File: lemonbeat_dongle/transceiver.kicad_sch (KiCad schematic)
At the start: 21 parts, among them J301 SMA, U301 Si4467, Y301 26MHz

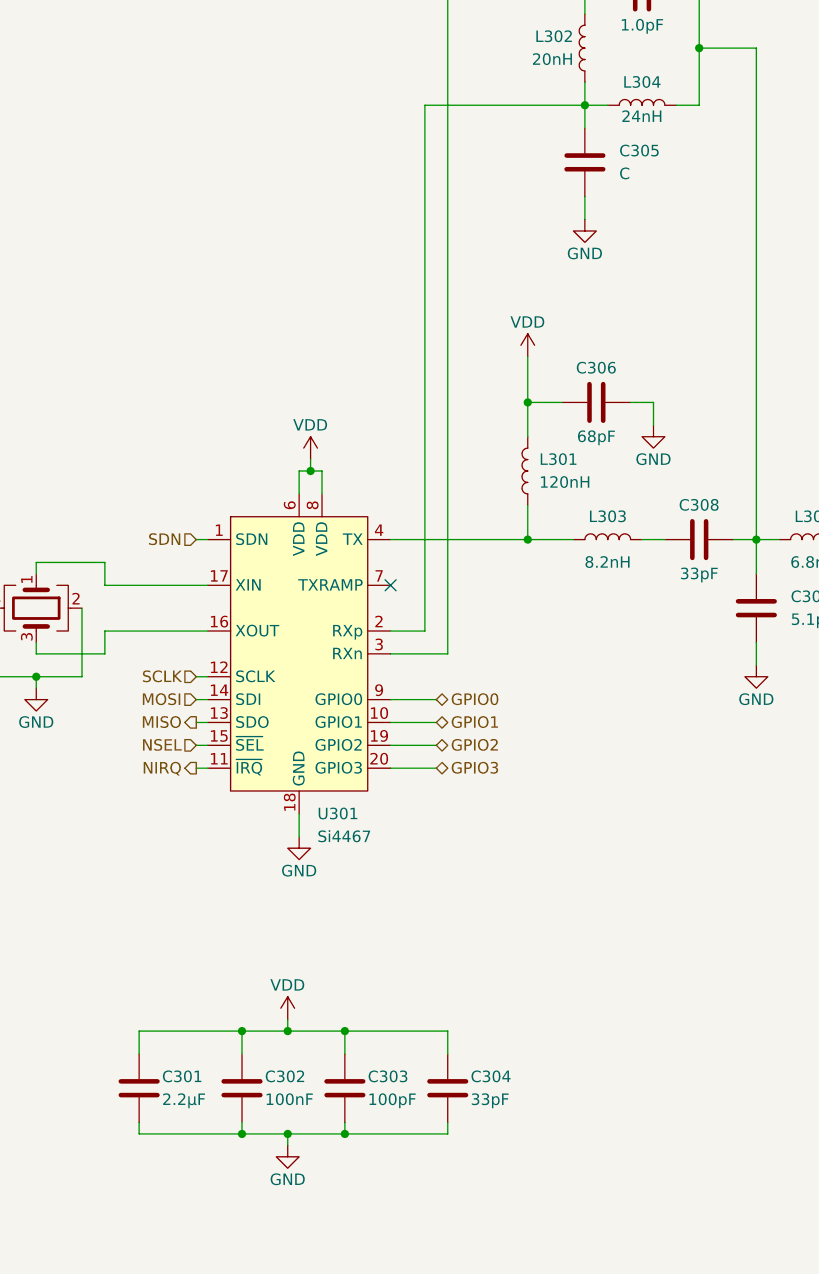
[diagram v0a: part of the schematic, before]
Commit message: lemonbeat dongle: assign footprints & add LCSC part numbers
Needs to be double-checked.
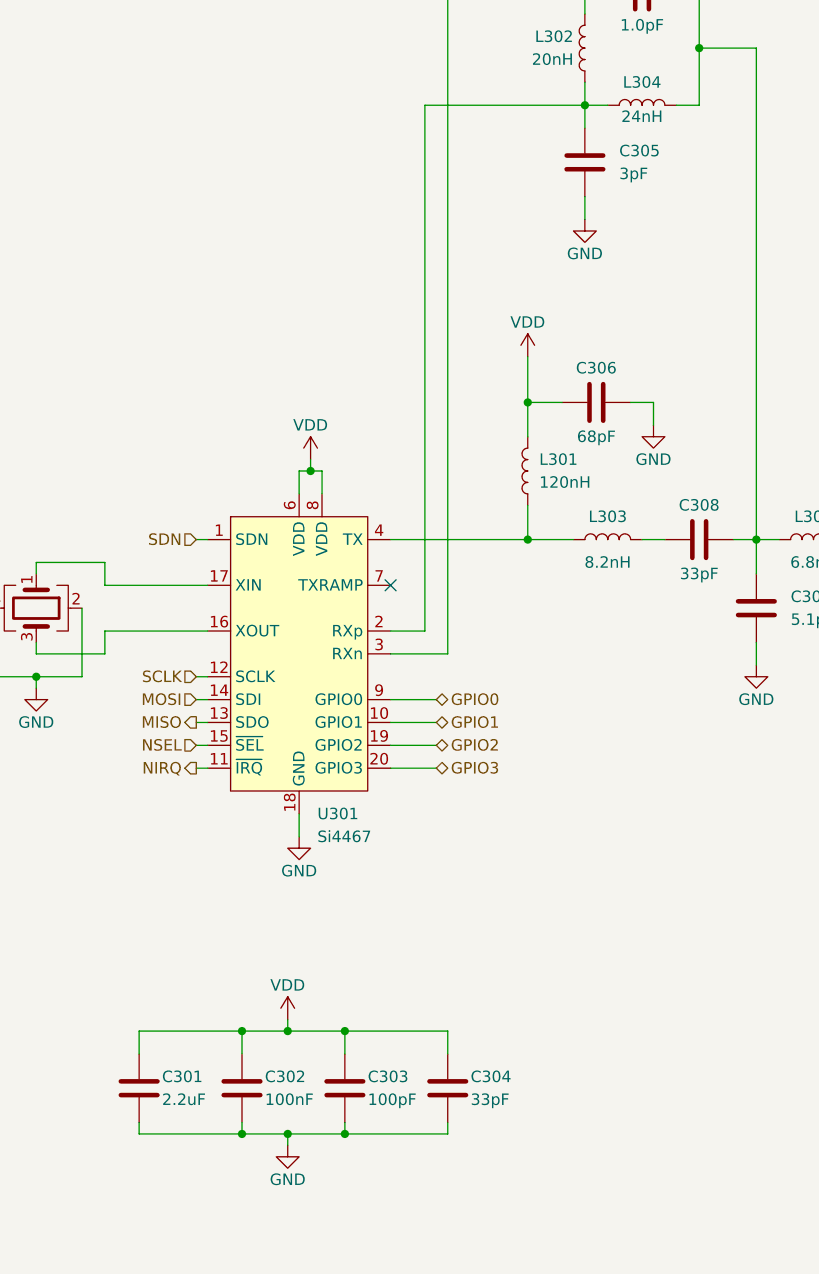
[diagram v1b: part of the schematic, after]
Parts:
- C301: value 2.2μF -> 2.2uF; footprint (none) -> Resistor_SMD:R_0402_1005Metric; Comment (none) -> JLCPCB basic part; LCSC (none) -> C12530; Manufacturer (none) -> Samsung Electro-Mechanics; Part Number (none) -> CL05A225MQ5NSNC
- C302: footprint (none) -> Resistor_SMD:R_0201_0603Metric; LCSC (none) -> C76939; Manufacturer (none) -> Murata Electronics; Part Number (none) -> GRM033R61E104KE14D
- C303: footprint (none) -> Resistor_SMD:R_0201_0603Metric; LCSC (none) -> C76922; Manufacturer (none) -> Murata Electronics; Part Number (none) -> GRM0335C1H101JA01D
- C304, C308: footprint (none) -> Resistor_SMD:R_0201_0603Metric; LCSC (none) -> C513616; Manufacturer (none) -> YAGEO; Part Number (none) -> CC0201JRNPO8BN330
- C305: value C -> 3pF; footprint (none) -> Resistor_SMD:R_0201_0603Metric; LCSC (none) -> C161388; Manufacturer (none) -> Murata Electronics; Part Number (none) -> GRM0335C1E3R0CA01D
- C306, C312: footprint (none) -> Resistor_SMD:R_0201_0603Metric; LCSC (none) -> C161433; Manufacturer (none) -> Murata Electronics; Part Number (none) -> GRM0335C1H680GA01D
- C307: footprint (none) -> Resistor_SMD:R_0201_0603Metric; LCSC (none) -> C723324; Manufacturer (none) -> Murata Electronics; Part Number (none) -> GJM0335C1H1R0WB01D
- C309, C311: footprint (none) -> Resistor_SMD:R_0201_0603Metric; LCSC (none) -> C441749; Manufacturer (none) -> Murata Electronics; Part Number (none) -> GRM0335C1H5R1BA01D
- C310: footprint (none) -> Resistor_SMD:R_0201_0603Metric; LCSC (none) -> C161369; Manufacturer (none) -> Murata Electronics; Part Number (none) -> GRM0335C1E100GA01D
- J301: footprint (none) -> Connector_Coaxial:SMA_Amphenol_132289_EdgeMount
- L301: footprint (none) -> Inductor_SMD:L_0402_1005Metric; LCSC (none) -> C335569; Manufacturer (none) -> Coilcraft; Part Number (none) -> 0402DC-R12XGRW
- L302: footprint (none) -> Inductor_SMD:L_0603_1608Metric; LCSC (none) -> C98070; Manufacturer (none) -> Murata Electronics; Part Number (none) -> LQW18AN20NJ00D
- L303: footprint (none) -> Inductor_SMD:L_0402_1005Metric; LCSC (none) -> C87185; Manufacturer (none) -> Taiyo Yuden; Part Number (none) -> HK10058N2J-T
- L304: footprint (none) -> Inductor_SMD:L_0402_1005Metric; LCSC (none) -> C167472; Manufacturer (none) -> Murata Electronics; Part Number (none) -> LQW15AN24NG00D
- L305, L306: footprint (none) -> Inductor_SMD:L_0402_1005Metric; LCSC (none) -> C335566; Manufacturer (none) -> Coilcraft; Part Number (none) -> 0402DC-6N8XGRW
- Y301: footprint (none) -> Crystal:Crystal_SMD_2016-4Pin_2.0x1.6mm

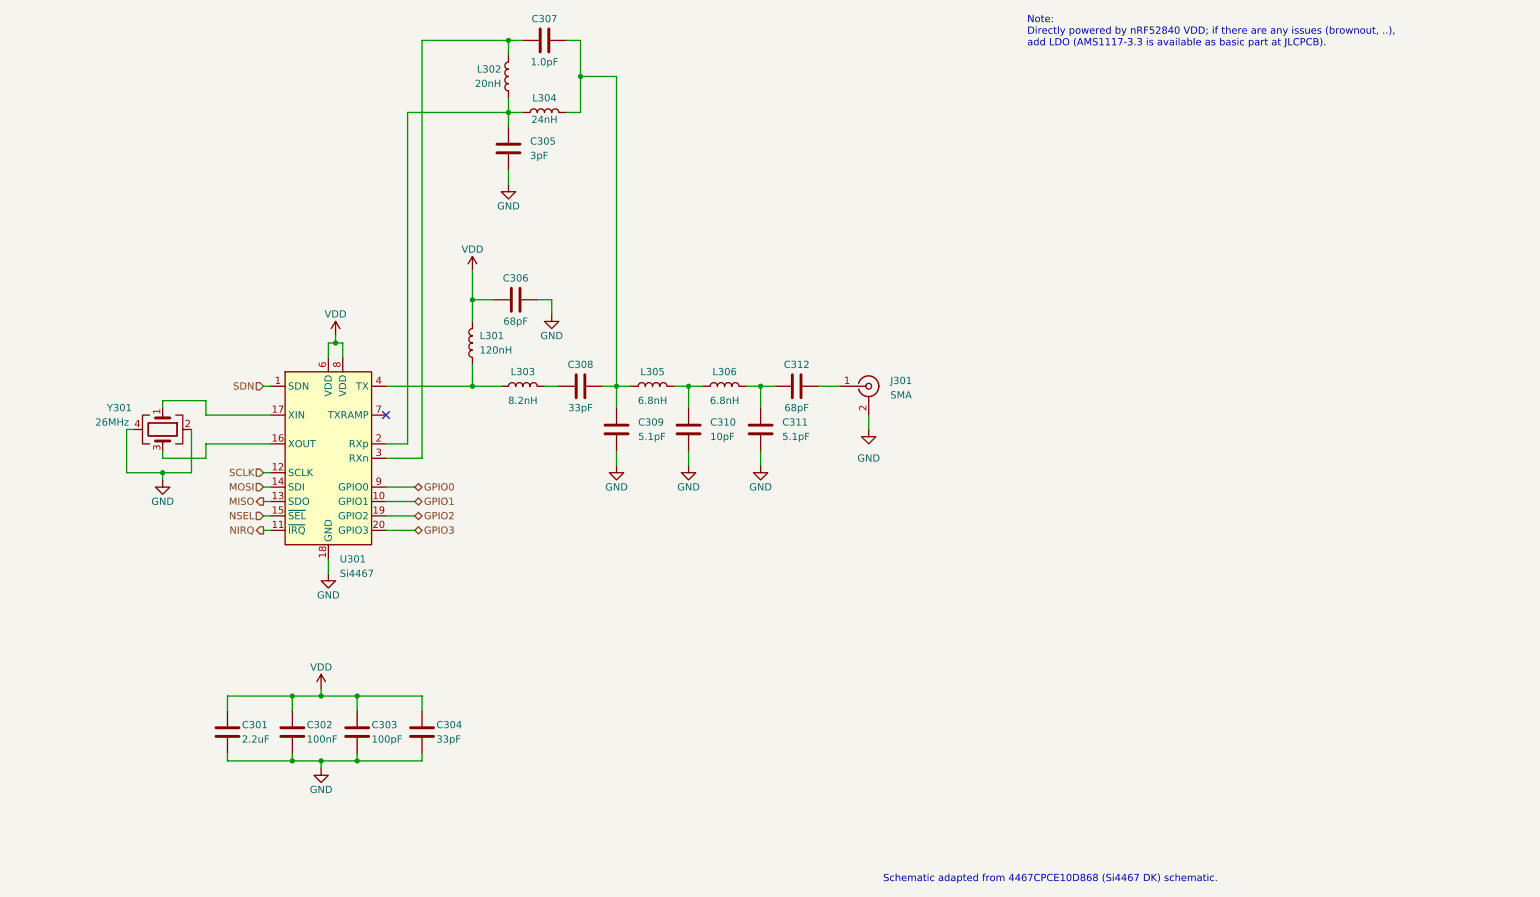
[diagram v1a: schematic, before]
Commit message: dongle: schematic: notes & cosmetic changes
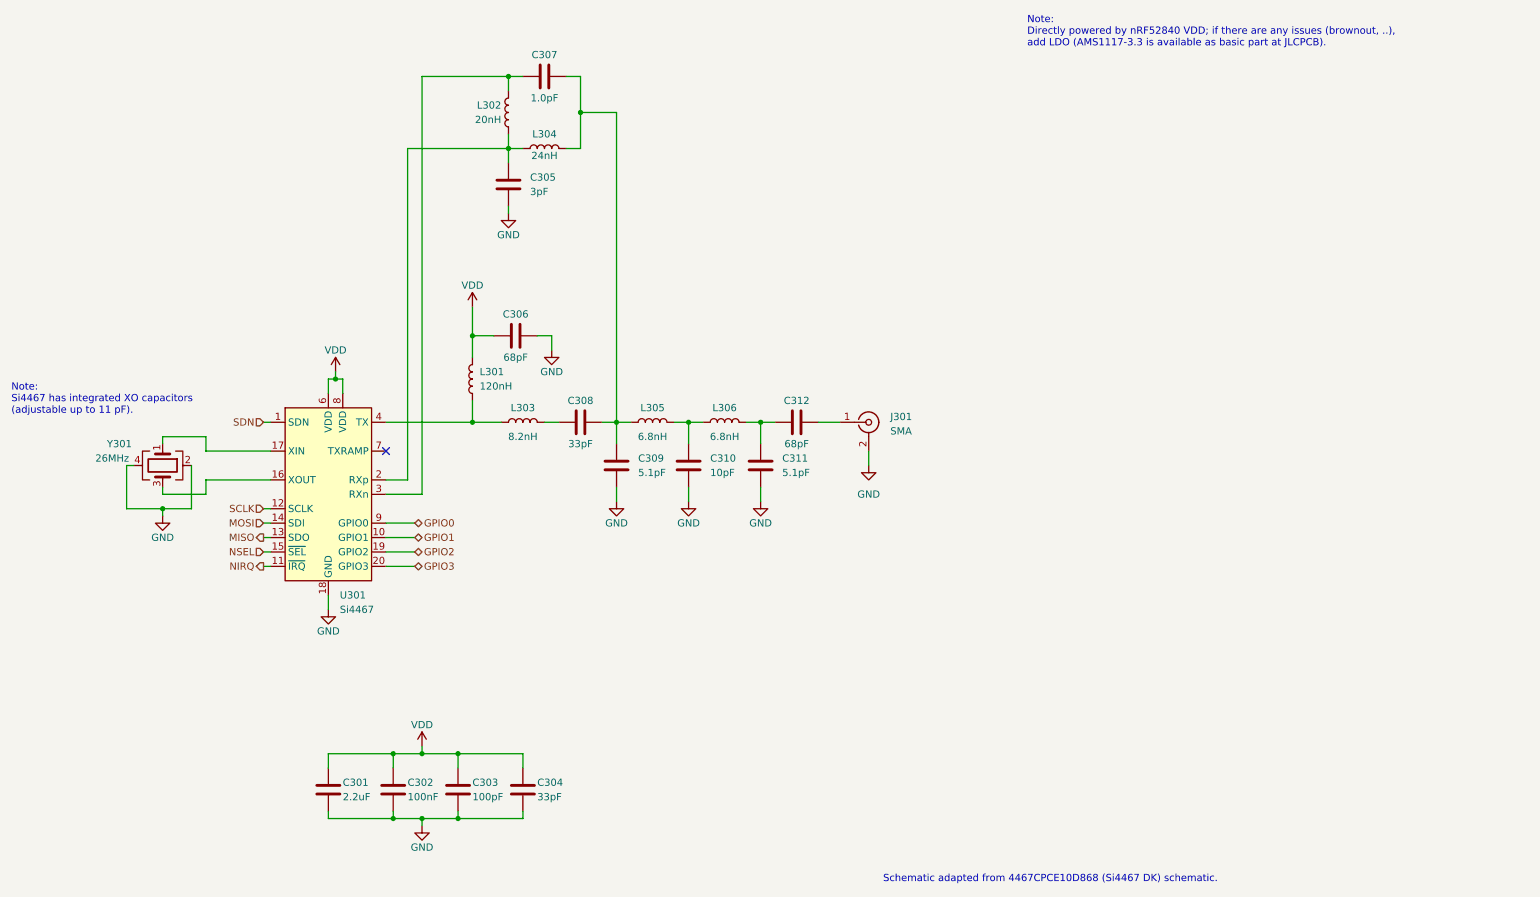
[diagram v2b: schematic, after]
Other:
- note added: "Note: Si4467 has integrated XO capacitors (adjustable up to 11 pF)."
- title: (none) -> Sub-GHz Transceiver
- moved on the sheet: C301, C302, C303, C304, C305, C306, C307, C308, C309, C310, C311, C312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

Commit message: dongle: use capacitor footprints for capacitors
(rather than identical resistor footprints)
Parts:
- C301: footprint Resistor_SMD:R_0402_1005Metric -> Capacitor_SMD:C_0402_1005Metric
- C302, C303, C304, C305, C306, C307, C308, C309, C310, C311, C312: footprint Resistor_SMD:R_0201_0603Metric -> Capacitor_SMD:C_0201_0603Metric
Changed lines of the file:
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@@
       (effects (font (size 1.27 1.27)) (justify left))
     )
-    (property "Footprint" "Resistor_SMD:R_0201_0603Metric" (id 2) (at 145.7452 100.33 0)
+    (property "Footprint" "Capacitor_SMD:C_0201_0603Metric" (id 2) (at 145.7452 100.33 0)
       (effects (font (size 1.27 1.27)) hide)
     )
@@
       (effects (font (size 1.27 1.27)) (justify left))
     )
-    (property "Footprint" "Resistor_SMD:R_0402_1005Metric" (id 2) (at 82.2452 157.48 0)
+    (property "Footprint" "Capacitor_SMD:C_0402_1005Metric" (id 2) (at 82.2452 157.48 0)
       (effects (font (size 1.27 1.27)) hide)
     )
@@
     (property "Reference" "C307" (id 0) (at 119.38 24.13 90))
     (property "Value" "1.0pF" (id 1) (at 119.38 31.75 90))
-    (property "Footprint" "Resistor_SMD:R_0201_0603Metric" (id 2) (at 123.19 26.9748 0)
+    (property "Footprint" "Capacitor_SMD:C_0201_0603Metric" (id 2) (at 123.19 26.9748 0)
       (effects (font (size 1.27 1.27)) hide)
     )
@@
       (effects (font (size 1.27 1.27)) (justify left))
     )
-    (property "Footprint" "Resistor_SMD:R_0201_0603Metric" (id 2) (at 113.9952 50.8 0)
+    (property "Footprint" "Capacitor_SMD:C_0201_0603Metric" (id 2) (at 113.9952 50.8 0)
       (effects (font (size 1.27 1.27)) hide)
     )
@@
       (effects (font (size 1.27 1.27)) (justify left))
     )
-    (property "Footprint" "Resistor_SMD:R_0201_0603Metric" (id 2) (at 116.5352 157.48 0)
+    (property "Footprint" "Capacitor_SMD:C_0201_0603Metric" (id 2) (at 116.5352 157.48 0)
       (effects (font (size 1.27 1.27)) hide)
     )
@@
     (property "Reference" "C308" (id 0) (at 125.73 85.09 90))
     (property "Value" "33pF" (id 1) (at 125.73 92.71 90))
-    (property "Footprint" "Resistor_SMD:R_0201_0603Metric" (id 2) (at 129.54 87.9348 0)
+    (property "Footprint" "Capacitor_SMD:C_0201_0603Metric" (id 2) (at 129.54 87.9348 0)
       (effects (font (size 1.27 1.27)) hide)
     )
@@
       (effects (font (size 1.27 1.27)) (justify left))
     )
-    (property "Footprint" "Resistor_SMD:R_0201_0603Metric" (id 2) (at 133.0452 100.33 0)
+    (property "Footprint" "Capacitor_SMD:C_0201_0603Metric" (id 2) (at 133.0452 100.33 0)
       (effects (font (size 1.27 1.27)) hide)
     )
@@
       (effects (font (size 1.27 1.27)) (justify left))
     )
-    (property "Footprint" "Resistor_SMD:R_0201_0603Metric" (id 2) (at 158.4452 100.33 0)
+    (property "Footprint" "Capacitor_SMD:C_0201_0603Metric" (id 2) (at 158.4452 100.33 0)
       (effects (font (size 1.27 1.27)) hide)
     )
@@
     (property "Reference" "C306" (id 0) (at 114.3 69.85 90))
     (property "Value" "68pF" (id 1) (at 114.3 77.47 90))
-    (property "Footprint" "Resistor_SMD:R_0201_0603Metric" (id 2) (at 118.11 72.6948 0)
+    (property "Footprint" "Capacitor_SMD:C_0201_0603Metric" (id 2) (at 118.11 72.6948 0)
       (effects (font (size 1.27 1.27)) hide)
     )
@@
       (effects (font (size 1.27 1.27)) (justify left))
     )
-    (property "Footprint" "Resistor_SMD:R_0201_0603Metric" (id 2) (at 105.1052 157.48 0)
+    (property "Footprint" "Capacitor_SMD:C_0201_0603Metric" (id 2) (at 105.1052 157.48 0)
       (effects (font (size 1.27 1.27)) hide)
     )
@@
     (property "Reference" "C312" (id 0) (at 163.83 85.09 90))
     (property "Value" "68pF" (id 1) (at 163.83 92.71 90))
-    (property "Footprint" "Resistor_SMD:R_0201_0603Metric" (id 2) (at 167.64 87.9348 0)
+    (property "Footprint" "Capacitor_SMD:C_0201_0603Metric" (id 2) (at 167.64 87.9348 0)
       (effects (font (size 1.27 1.27)) hide)
     )
@@
       (effects (font (size 1.27 1.27)) (justify left))
     )
-    (property "Footprint" "Resistor_SMD:R_0201_0603Metric" (id 2) (at 93.6752 157.48 0)
-      (effects (font (size 1.27 1.27)) hide)
-    )
+    (property "Footprint" "Capacitor_SMD:C_0201_0603Metric" (id 2) (at 93.6752 157.48 0)
+      (effects (font (size 1.27 1.27)) hide)
+    )
